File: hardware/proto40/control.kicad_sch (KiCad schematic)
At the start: 19 parts, among them U301 74AHCT125, U302 74AHCT125, U303 74LVC1G125, U304 74AHCT1G125

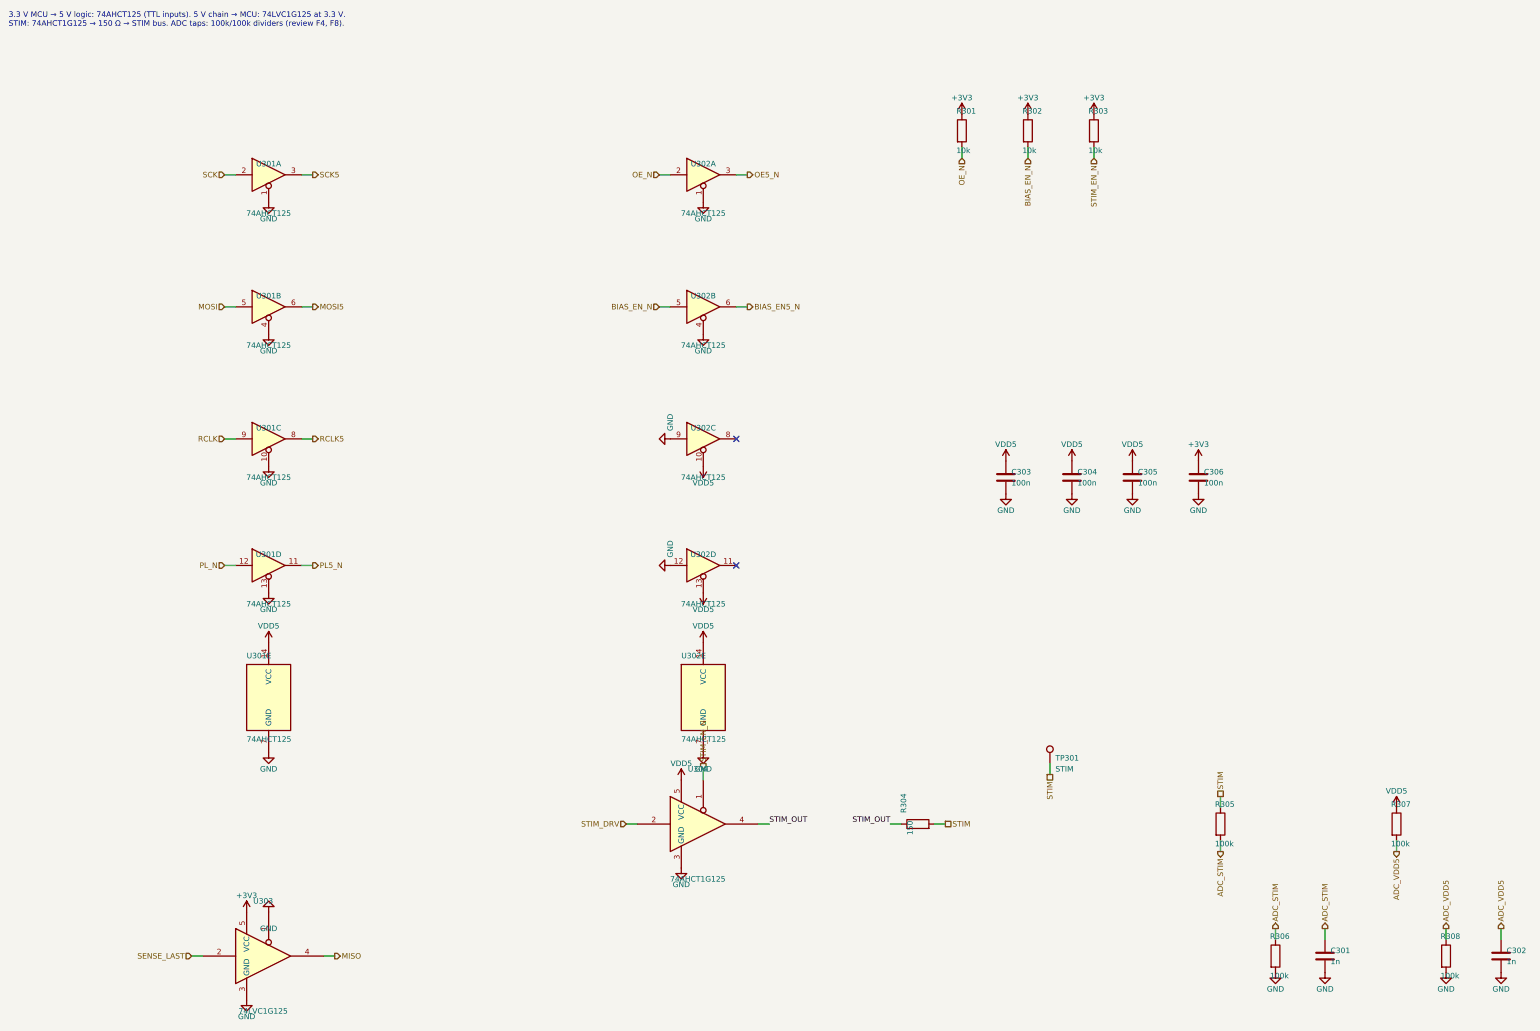
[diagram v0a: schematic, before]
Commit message: Redraw Proto40 schematic with wired functional blocks
Review feedback: text overlapped components and parts were isolated
islands joined only by labels, so connectivity was hard to follow.

- Generator: polyline wires, automatic junctions, text placement from
  the real symbol body graphics, KiCad field-angle handling for rotated
  symbols, power symbols oriented normally on horizontal pins
- Sheets redrawn left-to-right with wired blocks: channel cells, BIAS
  rail, decoupling on IC power pins, pull-ups on their lines, control
  ladder across the six groups, visible 165 chain, wired root hierarchy
  (MCU -> Control -> both sides) and cross-side LOOP
- layoutcheck.py: rejects text/text, text/body, text/wire overlaps and
  wires through bodies; CI runs the generator with --strict
- check_proto40.py: finds parts by sheet path and follows pins, so it no
  longer depends on net names or reference numbering

ERC 0 violations, design-intent audit PASS, layout issues 0.

Co-Authored-By: Claude Opus 5.5 <noreply@anthropic.com>
Claude-Session: https://claude.ai/code/session_01UG7pR5ZtgvoVGRWFojzQKf
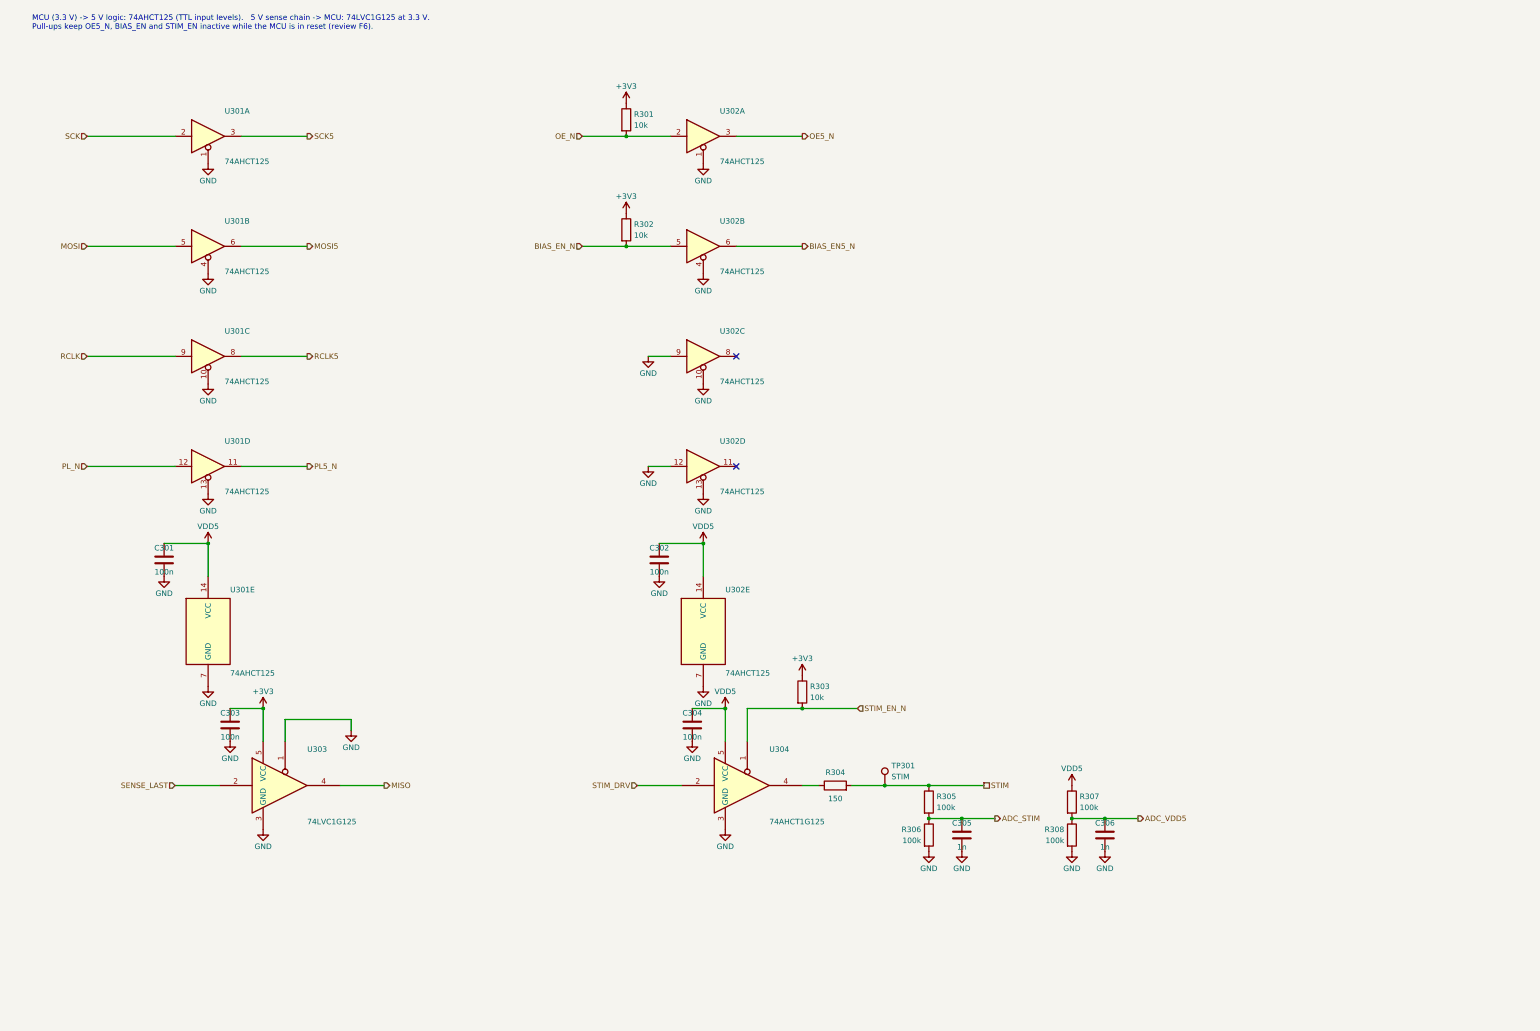
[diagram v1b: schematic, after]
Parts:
- C301, C302: value 1n -> 100n
- C305, C306: value 100n -> 1n
- R301, R302: Note safe default during MCU reset -> inactive during MCU reset
- R303: Note safe default during MCU reset -> stimulus off during MCU reset
- U301, U302: Manufacturer (none) -> Texas Instruments
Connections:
- net +3V3: now also C303.1; no longer C306.1
- net ADC_STIM: now also C305.1; no longer C301.1
- net ADC_VDD5: now also C306.1; no longer C302.1
- net GND: now also U302.10, U302.13
- net VDD5: now also C301.1, C302.1; no longer C303.1, C305.1, U302.10, U302.13
- net STIM_OUT: no longer names the net of R304.1, U304.4
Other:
- note added: "MCU (3.3 V) -> 5 V logic: 74AHCT125 (TTL input levels). 5 V sense chain -> MCU: 74LVC1G125 at 3.3 V. Pull-ups keep OE5_N, BIAS_EN and STIM_EN inactive while the MCU is in reset (review F6)."
- note removed: "3.3 V MCU → 5 V logic: 74AHCT125 (TTL inputs). 5 V chain → MCU: 74LVC1G125 at 3.3 V. STIM: 74AHCT1G125 → 150 Ω → STIM bus. ADC taps: 100k/100k dividers (review F4, F8)."
- moved on the sheet: C301, C302, C303, C304, C305, C306, R301, R302, R303, R304, R305, R306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
